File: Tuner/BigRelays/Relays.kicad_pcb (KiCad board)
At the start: 2 copper layers, 100 x 100 mm, 93 parts, among them J1 Conn_01x03, J10 Conn_01x02, J11 Conn_01x02, J12 Conn_01x01, J13 Conn_01x01, J14 Conn_01x01, J15 Conn_01x01, J16 Conn_01x02, J17 Conn_02x10_Odd_Even, J18 Conn_01x02, J19 Conn_01x03, J2 Conn_01x03, J21 Conn_01x01, J22 Conn_01x01, J23 Conn_01x01, J24 Conn_01x01, J25 Conn_01x01, J27 Conn_01x01, J28 Conn_01x01, J29 Conn_01x01, J3 Conn_01x03, J30 Conn_01x01, J4 Conn_01x03, J5 Conn_01x03, J6 Conn_01x03, J7 Conn_01x03, J8 Conn_01x02, J9 Conn_01x02

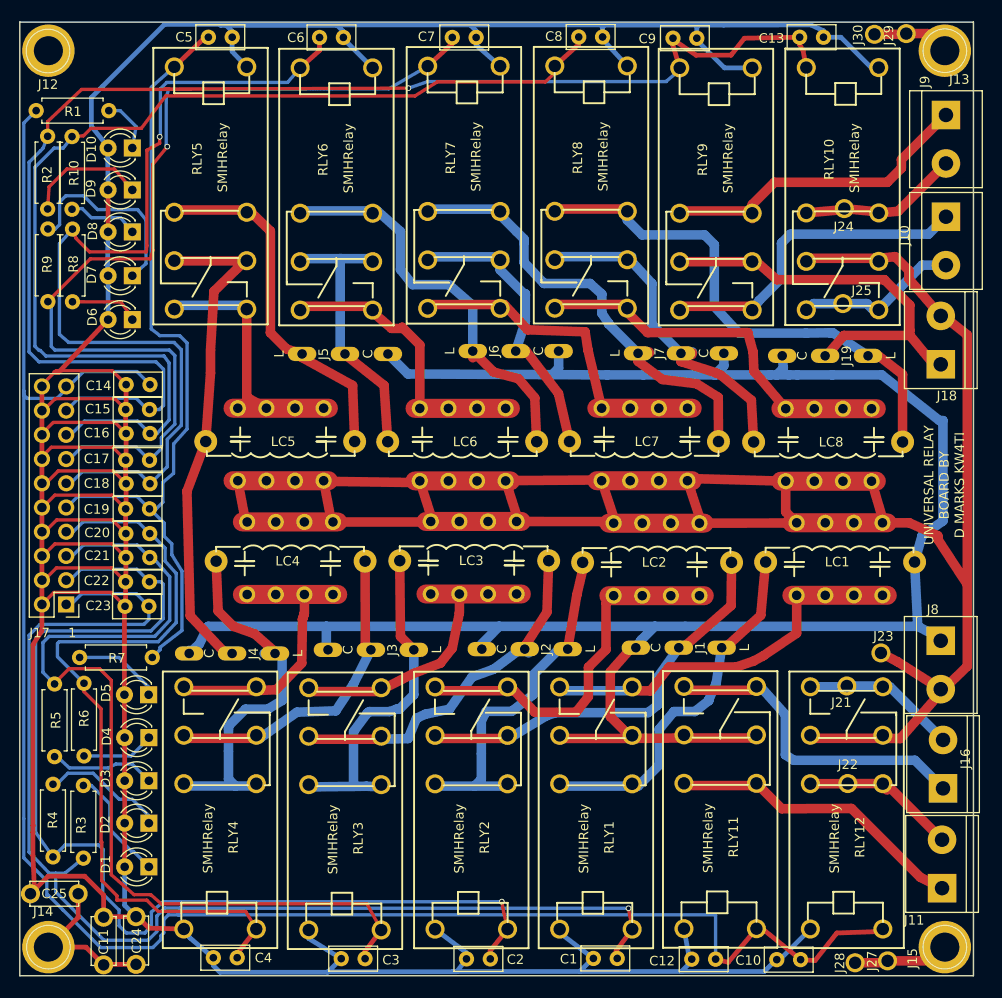
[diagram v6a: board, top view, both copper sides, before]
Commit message: Added extra capacitors between relay power and ground posts
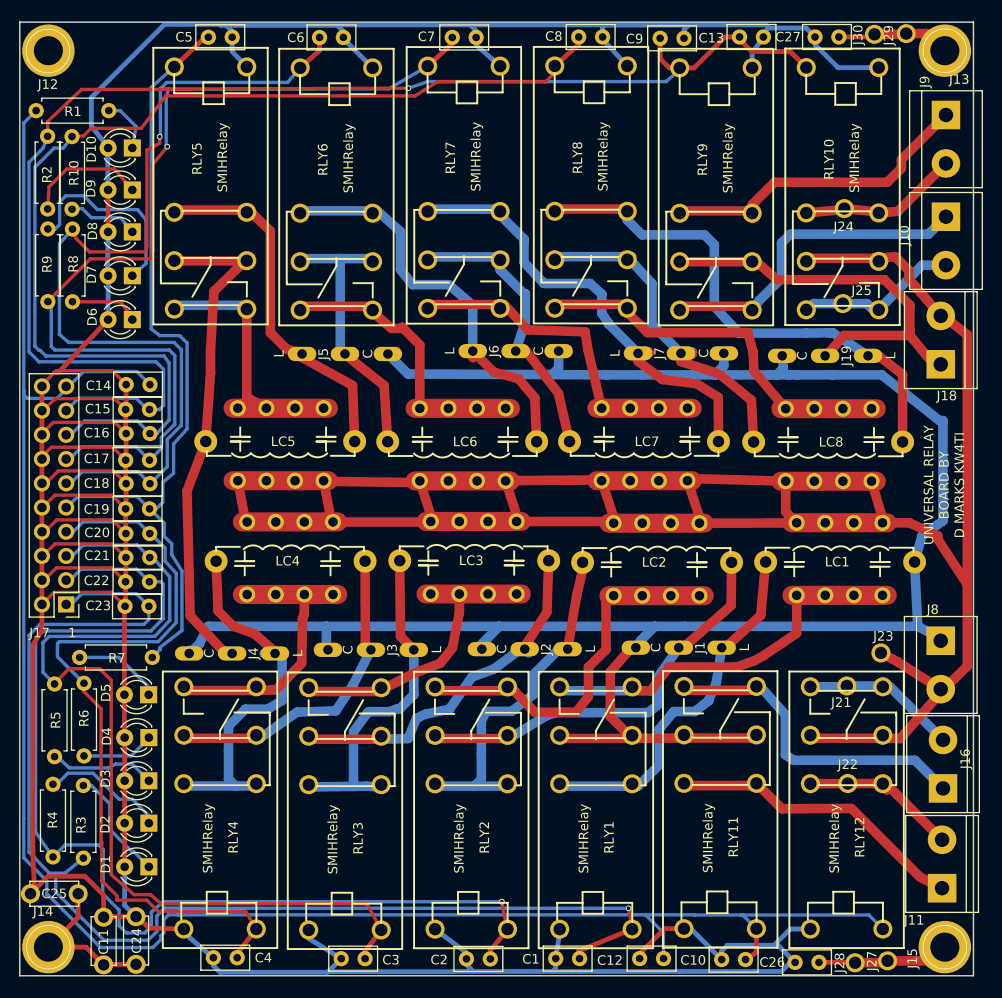
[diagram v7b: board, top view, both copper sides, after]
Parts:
- added C26: 10 nF, Capacitors_THT:C_Disc_D5.0mm_W2.5mm_P2.50mm, F.Cu at (133.8, 148.6)
- added C27: 10 nF, Capacitors_THT:C_Disc_D5.0mm_W2.5mm_P2.50mm, F.Cu at (135.9, 51.6)
- moved C13 6.30 mm to (125.5, 51.6)
- moved C10 5.78 mm to (126.1, 148.3)
- moved C12 5.46 mm to (117.5, 148.2)
- moved C1 3.95 mm to (108.7, 148.2)
- moved C9 1.34 mm to (117.2, 51.7)
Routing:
- net +5V: track 481.5 -> 496.3 mm
- net Net-(C27-Pad1): track 11.2 -> 15.1 mm
- net Net-(C26-Pad1): track 12.7 -> 16.5 mm
- net RLY10: track 201.1 -> 204.5 mm
- net RLY1: track 126.6 -> 129.9 mm
- net RLY9: track 146.3 -> 145.7 mm

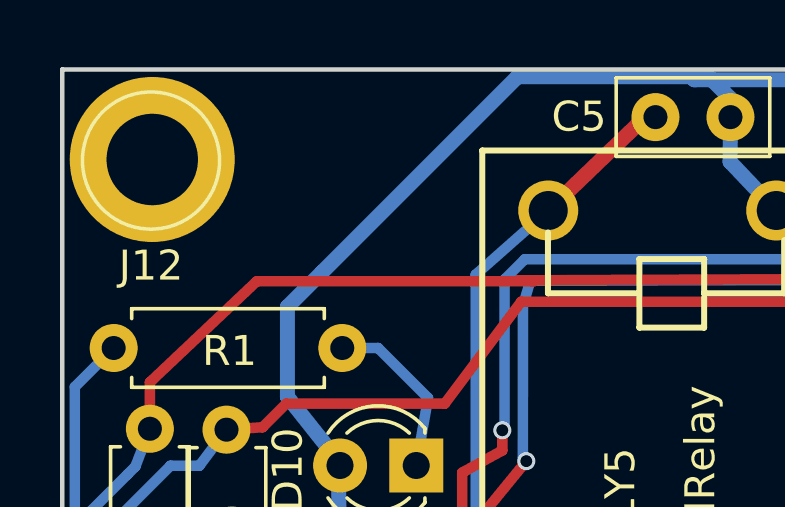
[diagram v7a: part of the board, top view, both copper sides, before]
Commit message: Added extra capacitors to ground to large relay boards
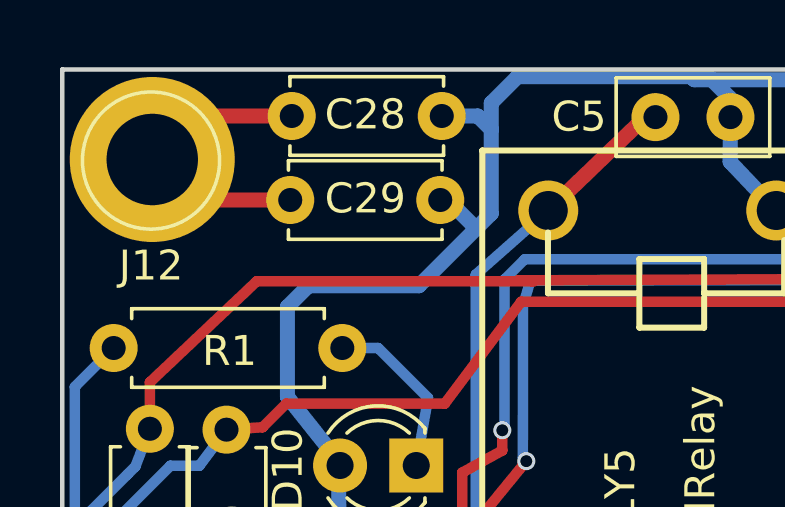
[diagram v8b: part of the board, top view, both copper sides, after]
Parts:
- added C28: 10 nF, Capacitors_THT:C_Disc_D5.0mm_W2.5mm_P5.00mm, F.Cu at (57.6, 51.5)
- added C29: 10 nF, Capacitors_THT:C_Disc_D5.0mm_W2.5mm_P5.00mm, F.Cu at (57.6, 54.4)
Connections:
- J12 pad 1: (no net) -> Net-(C28-Pad1)
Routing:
- net Net-(C28-Pad1): track 0.00 -> 10.4 mm
- net +5V: track 496.3 -> 501.9 mm
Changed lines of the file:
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@@
 (kicad_pcb (version 4) (host pcbnew 4.0.7)
   (general
-    (links 296)
+    (links 300)
     (no_connects 0)
-    (area 44.941618 46.95878 152.967 152.888419)
+    (area 49.924999 49.924999 150.075001 150.075001)
     (thickness 1.6)
     (drawings 30)
-    (tracks 1054)
+    (tracks 1067)
     (zones 0)
-    (modules 95)
-    (nets 59)
+    (modules 97)
+    (nets 60)
   )
   (page A4)
@@
   (net 57 "Net-(C26-Pad1)")
   (net 58 "Net-(C27-Pad1)")
+  (net 59 "Net-(C28-Pad1)")
   (net_class Default "This is the default net class."
     (clearance 0.2)
@@
     (add_net "Net-(C26-Pad1)")
     (add_net "Net-(C27-Pad1)")
+    (add_net "Net-(C28-Pad1)")
     (add_net "Net-(D1-Pad1)")
     (add_net "Net-(D10-Pad1)")
@@
     (fp_circle (center 0 0) (end 2.6 0) (layer F.CrtYd) (width 0.05))
     (fp_circle (center 0 0) (end 0 -2.286) (layer F.SilkS) (width 0.12))
-    (pad 1 thru_hole circle (at 0.041 -0.0352) (size 5.5 5.5) (drill 3.048) (layers *.Cu *.Mask))
+    (pad 1 thru_hole circle (at 0.041 -0.0352) (size 5.5 5.5) (drill 3.048) (layers *.Cu *.Mask)
+      (net 59 "Net-(C28-Pad1)"))
   )
   (module Capacitors_THT:C_Disc_D5.0mm_W2.5mm_P5.00mm (layer F.Cu)
@@
     )
   )
+  (module Capacitors_THT:C_Disc_D5.0mm_W2.5mm_P5.00mm (layer F.Cu)
+    (at 57.65 51.55)
+    (descr "C, Disc series, Radial, pin pitch=5.00mm, , diameter*width=5*2.5mm^2, Capacitor, http://cdn-reichelt.de/documents/datenblatt/B300/DS_KERKO_TC.pdf")
+    (tags "C Disc series Radial pin pitch 5.00mm  diameter 5mm width 2.5mm Capacitor")
+    (fp_text reference C28 (at 2.45 -0.05) (layer F.SilkS)
+      (effects (font (size 1 1) (thickness 0.15)))
+    )
+    (fp_text value "10 nF" (at 2.5 2.56) (layer F.Fab)
+      (effects (font (size 1 1) (thickness 0.15)))
+    )
+    (fp_line (start 0 -1.25) (end 0 1.25) (layer F.Fab) (width 0.1))
+    (fp_line (start 0 1.25) (end 5 1.25) (layer F.Fab) (width 0.1))
+    (fp_line (start 5 1.25) (end 5 -1.25) (layer F.Fab) (width 0.1))
+    (fp_line (start 5 -1.25) (end 0 -1.25) (layer F.Fab) (width 0.1))
+    (fp_line (start -0.06 -1.31) (end 5.06 -1.31) (layer F.SilkS) (width 0.12))
+    (fp_line (start -0.06 1.31) (end 5.06 1.31) (layer F.SilkS) (width 0.12))
+    (fp_line (start -0.06 -1.31) (end -0.06 -0.996) (layer F.SilkS) (width 0.12))
+    (fp_line (start -0.06 0.996) (end -0.06 1.31) (layer F.SilkS) (width 0.12))
+    (fp_line (start 5.06 -1.31) (end 5.06 -0.996) (layer F.SilkS) (width 0.12))
+    (fp_line (start 5.06 0.996) (end 5.06 1.31) (layer F.SilkS) (width 0.12))
+    (fp_line (start -1.05 -1.6) (end -1.05 1.6) (layer F.CrtYd) (width 0.05))
+    (fp_line (start -1.05 1.6) (end 6.05 1.6) (layer F.CrtYd) (width 0.05))
+    (fp_line (start 6.05 1.6) (end 6.05 -1.6) (layer F.CrtYd) (width 0.05))
+    (fp_line (start 6.05 -1.6) (end -1.05 -1.6) (layer F.CrtYd) (width 0.05))
+    (fp_text user %R (at 2.5 0) (layer F.Fab)
+      (effects (font (size 1 1) (thickness 0.15)))
+    )
+    (pad 1 thru_hole circle (at 0 0) (size 1.6 1.6) (drill 0.8) (layers *.Cu *.Mask)
+      (net 59 "Net-(C28-Pad1)"))
+    (pad 2 thru_hole circle (at 5 0) (size 1.6 1.6) (drill 0.8) (layers *.Cu *.Mask)
+      (net 32 +5V))
+    (model ${KISYS3DMOD}/Capacitors_THT.3dshapes/C_Disc_D5.0mm_W2.5mm_P5.00mm.wrl
+      (at (xyz 0 0 0))
+      (scale (xyz 1 1 1))
+      (rotate (xyz 0 0 0))
+    )
+  )
+  (module Capacitors_THT:C_Disc_D5.0mm_W2.5mm_P5.00mm (layer F.Cu)
+    (at 57.6 54.35)
+    (descr "C, Disc series, Radial, pin pitch=5.00mm, , diameter*width=5*2.5mm^2, Capacitor, http://cdn-reichelt.de/documents/datenblatt/B300/DS_KERKO_TC.pdf")
+    (tags "C Disc series Radial pin pitch 5.00mm  diameter 5mm width 2.5mm Capacitor")
+    (fp_text reference C29 (at 2.5 -0.05) (layer F.SilkS)
+      (effects (font (size 1 1) (thickness 0.15)))
+    )
+    (fp_text value "10 nF" (at 2.5 2.56) (layer F.Fab)
+      (effects (font (size 1 1) (thickness 0.15)))
+    )
+    (fp_line (start 0 -1.25) (end 0 1.25) (layer F.Fab) (width 0.1))
+    (fp_line (start 0 1.25) (end 5 1.25) (layer F.Fab) (width 0.1))
+    (fp_line (start 5 1.25) (end 5 -1.25) (layer F.Fab) (width 0.1))
+    (fp_line (start 5 -1.25) (end 0 -1.25) (layer F.Fab) (width 0.1))
+    (fp_line (start -0.06 -1.31) (end 5.06 -1.31) (layer F.SilkS) (width 0.12))
+    (fp_line (start -0.06 1.31) (end 5.06 1.31) (layer F.SilkS) (width 0.12))
+    (fp_line (start -0.06 -1.31) (end -0.06 -0.996) (layer F.SilkS) (width 0.12))
+    (fp_line (start -0.06 0.996) (end -0.06 1.31) (layer F.SilkS) (width 0.12))
+    (fp_line (start 5.06 -1.31) (end 5.06 -0.996) (layer F.SilkS) (width 0.12))
+    (fp_line (start 5.06 0.996) (end 5.06 1.31) (layer F.SilkS) (width 0.12))
+    (fp_line (start -1.05 -1.6) (end -1.05 1.6) (layer F.CrtYd) (width 0.05))
+    (fp_line (start -1.05 1.6) (end 6.05 1.6) (layer F.CrtYd) (width 0.05))
+    (fp_line (start 6.05 1.6) (end 6.05 -1.6) (layer F.CrtYd) (width 0.05))
+    (fp_line (start 6.05 -1.6) (end -1.05 -1.6) (layer F.CrtYd) (width 0.05))
+    (fp_text user %R (at 2.5 0) (layer F.Fab)
+      (effects (font (size 1 1) (thickness 0.15)))
+    )
+    (pad 1 thru_hole circle (at 0 0) (size 1.6 1.6) (drill 0.8) (layers *.Cu *.Mask)
+      (net 59 "Net-(C28-Pad1)"))
+    (pad 2 thru_hole circle (at 5 0) (size 1.6 1.6) (drill 0.8) (layers *.Cu *.Mask)
+      (net 32 +5V))
+    (model ${KISYS3DMOD}/Capacitors_THT.3dshapes/C_Disc_D5.0mm_W2.5mm_P5.00mm.wrl
+      (at (xyz 0 0 0))
+      (scale (xyz 1 1 1))
+      (rotate (xyz 0 0 0))
+    )
+  )
   (gr_text GND (at 140.65504 114.38128) (layer B.SilkS)
     (effects (font (size 1 1) (thickness 0.15)) (justify mirror))
@@
   (segment (start 56.77408 91.83878) (end 62.34938 91.83878) (width 0.35) (layer B.Cu) (net 31))
   (segment (start 62.34938 91.83878) (end 63.6524 93.1418) (width 0.35) (layer B.Cu) (net 31) (status 20))
+  (segment (start 62.6 54.35) (end 62.85 54.35) (width 0.5) (layer B.Cu) (net 32) (status C00000))
+  (segment (start 62.85 54.35) (end 63.8 55.3) (width 0.5) (layer B.Cu) (net 32) (status 400000))
+  (segment (start 62.65 51.55) (end 63.85 51.55) (width 0.5) (layer B.Cu) (net 32) (status 400000))
+  (segment (start 63.85 51.55) (end 64.3 52) (width 0.5) (layer B.Cu) (net 32))
+  (segment (start 58.2088 57.2088) (end 61.8912 57.2088) (width 0.5) (layer B.Cu) (net 32))
+  (segment (start 64.3 54.8) (end 64.3 52) (width 0.5) (layer B.Cu) (net 32))
+  (segment (start 64.3 52) (end 64.3 51.1176) (width 0.5) (layer B.Cu) (net 32))
+  (segment (start 61.8912 57.2088) (end 63.8 55.3) (width 0.5) (layer B.Cu) (net 32))
+  (segment (start 63.8 55.3) (end 64.3 54.8) (width 0.5) (layer B.Cu) (net 32))
   (segment (start 133.39 51.562) (end 133.39 52.364) (width 0.5) (layer B.Cu) (net 32))
   (segment (start 135.796 54.77) (end 140.071 54.77) (width 0.5) (layer B.Cu) (net 32))
@@
   (segment (start 71.0692 50.3428) (end 71.0692 50.2412) (width 0.5) (layer B.Cu) (net 32))
   (segment (start 83.2866 50.3428) (end 71.0692 50.3428) (width 0.5) (layer B.Cu) (net 32))
-  (segment (start 65.1764 50.2412) (end 58.674 56.7436) (width 0.5) (layer B.Cu) (net 32))
+  (segment (start 65.1764 50.2412) (end 64.3 51.1176) (width 0.5) (layer B.Cu) (net 32))
   (segment (start 71.0692 50.2412) (end 65.1764 50.2412) (width 0.5) (layer B.Cu) (net 32))
-  (segment (start 58.674 56.7436) (end 57.5056 57.912) (width 0.5) (layer B.Cu) (net 32))
+  (segment (start 58.2088 57.2088) (end 57.5056 57.912) (width 0.5) (layer B.Cu) (net 32))
   (segment (start 136.30656 79.51724) (end 138.83132 79.51724) (width 1) (layer B.Cu) (net 33))
   (segment (start 138.83132 79.51724) (end 139.48408 80.17) (width 1) (layer B.Cu) (net 33))
@@
   (segment (start 146.533 53.467) (end 147 53) (width 1) (layer F.Cu) (net 58))
   (segment (start 145.308 51.308) (end 147 53) (width 0.5) (layer F.Cu) (net 58))
+  (segment (start 57.6 54.35) (end 54.35 54.35) (width 0.5) (layer F.Cu) (net 59) (status C00000))
+  (segment (start 54.35 54.35) (end 53 53) (width 0.5) (layer F.Cu) (net 59) (status C00000))
+  (segment (start 57.65 51.55) (end 54.45 51.55) (width 0.5) (layer F.Cu) (net 59) (status C00000))
+  (segment (start 54.45 51.55) (end 53 53) (width 0.5) (layer F.Cu) (net 59) (status C00000))
 )
